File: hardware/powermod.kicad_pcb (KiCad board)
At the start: 4 copper layers, 65 x 40 mm, 78 parts, among them J1 USB_C_IN, J2 USB_C_OUT, J3 JST_PH_2, J4 STEMMA_QT, J5 SWD_HDR, Q1 AON7407, Q2 AON7407, Q3 BSS138, SW1 BUTTON, U1 BM8563, U2 PY32F003F18P6, U3 TPS63020DSJR, U4 TP4056, U5 XC6206P332MR, Y1 32.768kHz

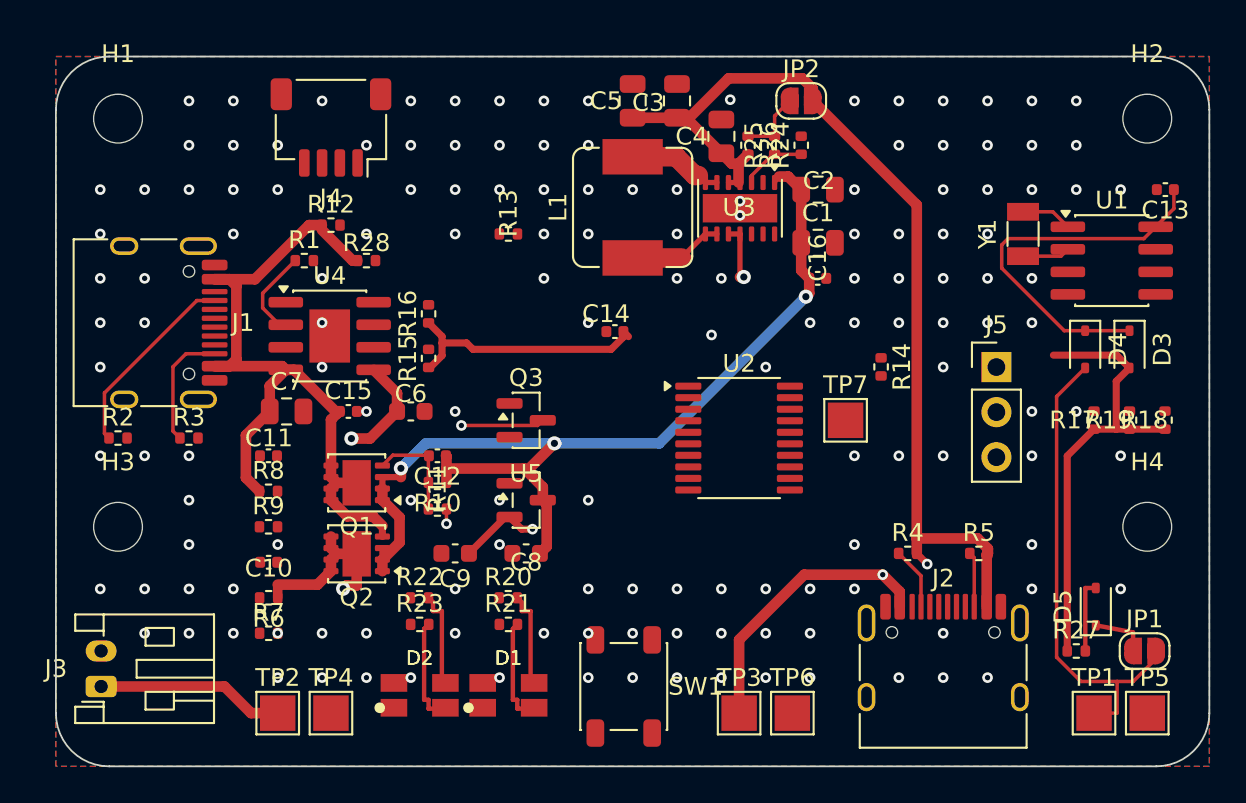
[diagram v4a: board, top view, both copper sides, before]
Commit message: hardware: user MCU/J3 placement + fix J3-flip VBAT short
User placed the TSSOP (36.5,22.5) and moved/rotated J3 to the exposed strip
(7.95,33). Flipping J3 swapped its pads, so the stale VBAT stubs to the old J3
spot shorted to the new GND pad — stripped those 6 tracks/vias. Board verified:
pad-diff 226/226, no courtyard collisions, DRC clean apart from the 4 known U3
track_width necks + 38 unrouted (MCU nets + J3 VBAT/GND). MCU-area routing TBD.

Co-Authored-By: Claude Opus 4.8 <noreply@anthropic.com>
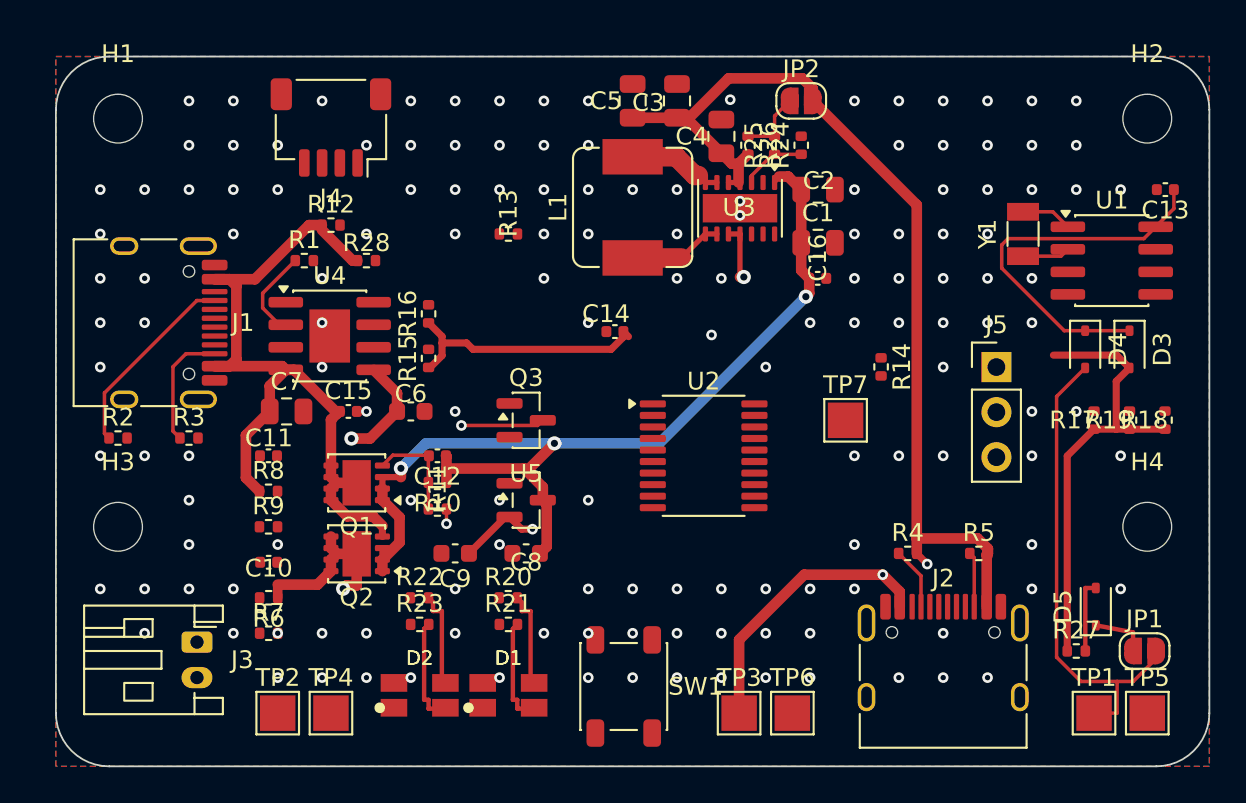
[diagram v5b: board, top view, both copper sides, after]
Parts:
- moved J3 5.95 mm to (7.95, 33.0), turned to -90 degrees
- moved U2 2.24 mm to (36.5, 22.5)
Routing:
- net VBAT: track 51.3 -> 24.8 mm
- net GND: vias 149 -> 148
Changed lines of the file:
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@@
 	(footprint "TSSOP-20_4.4x6.5mm_P0.65mm"
 		(layer "F.Cu")
-		(at 38.5 21.5)
+		(at 36.5 22.5)
 		(descr "TSSOP, 20 Pin (JEDEC MO-153 Var AC https://www.jedec.org/document_search?search_api_views_fulltext=MO-153)")
 		(tags "TSSOP SO")
@@
 	(footprint "JST_PH_S2B-PH-K_1x02_P2.00mm_Horizontal"
 		(layer "F.Cu")
-		(at 2.55 35.5 90)
+		(at 7.95 33 -90)
 		(descr "JST PH series connector, S2B-PH-K (http://www.jst-mfg.com/product/pdf/eng/ePH.pdf)")
 		(tags "connector JST PH horizontal")
@@
 		(duplicate_pad_numbers_are_jumpers no)
 		(fp_line
-			(start 4.06 -1.46)
-			(end 3.14 -1.46)
+			(start -2.06 6.36)
+			(end 4.06 6.36)
 			(stroke
 				(width 0.12)
@@
 		)
 		(fp_line
-			(start 3.14 -1.46)
-			(end 3.14 0.14)
+			(start 0.5 6.36)
+			(end 0.5 2)
 			(stroke
 				(width 0.12)
@@
 		)
 		(fp_line
-			(start -1.14 -1.46)
-			(end -2.06 -1.46)
+			(start 4.06 6.36)
+			(end 4.06 -1.46)
 			(stroke
 				(width 0.12)
@@
 		)
 		(fp_line
-			(start -2.06 -1.46)
-			(end -2.06 6.36)
+			(start -0.8 4.1)
+			(end -0.8 6.36)
 			(stroke
 				(width 0.12)
@@
 		)
 		(fp_line
-			(start 4.06 0.14)
-			(end 3.14 0.14)
+			(start -0.3 4.1)
+			(end -0.3 6.36)
 			(stroke
 				(width 0.12)
@@
 		)
 		(fp_line
-			(start 3.14 0.14)
-			(end 2.86 0.14)
+			(start 0.5 2)
+			(end 1.5 2)
 			(stroke
 				(width 0.12)
@@
 		)
 		(fp_line
-			(start -0.86 0.14)
-			(end -0.86 -1.075)
+			(start 1.5 2)
+			(end 1.5 6.36)
 			(stroke
 				(width 0.12)
@@
 		)
 		(fp_line
-			(start -0.86 0.14)
+			(start -2.06 0.14)
 			(end -1.14 0.14)
 			(stroke
@@
 		)
 		(fp_line
-			(start -2.06 0.14)
+			(start -0.86 0.14)
 			(end -1.14 0.14)
 			(stroke
@@
 		)
 		(fp_line
-			(start 1.5 2)
-			(end 1.5 6.36)
+			(start -0.86 0.14)
+			(end -0.86 -1.075)
 			(stroke
 				(width 0.12)
@@
 		)
 		(fp_line
-			(start 0.5 2)
-			(end 1.5 2)
+			(start 3.14 0.14)
+			(end 2.86 0.14)
 			(stroke
 				(width 0.12)
@@
 		)
 		(fp_line
-			(start -0.3 4.1)
-			(end -0.3 6.36)
+			(start 4.06 0.14)
+			(end 3.14 0.14)
 			(stroke
 				(width 0.12)
@@
 		)
 		(fp_line
-			(start -0.8 4.1)
-			(end -0.8 6.36)
+			(start -2.06 -1.46)
+			(end -2.06 6.36)
 			(stroke
 				(width 0.12)
@@
 		)
 		(fp_line
-			(start 4.06 6.36)
-			(end 4.06 -1.46)
+			(start -1.14 -1.46)
+			(end -2.06 -1.46)
 			(stroke
 				(width 0.12)
@@
 		)
 		(fp_line
-			(start 0.5 6.36)
-			(end 0.5 2)
+			(start 3.14 -1.46)
+			(end 3.14 0.14)
 			(stroke
 				(width 0.12)
@@
 		)
 		(fp_line
-			(start -2.06 6.36)
-			(end 4.06 6.36)
+			(start 4.06 -1.46)
+			(end 3.14 -1.46)
 			(stroke
 				(width 0.12)
@@
 		)
 		(fp_rect
-			(start 2.3 2.5)
-			(end 3.3 4.1)
+			(start -1.3 2.5)
+			(end -0.3 4.1)
 			(stroke
 				(width 0.12)
@@
 		)
 		(fp_rect
-			(start -1.3 2.5)
-			(end -0.3 4.1)
+			(start 2.3 2.5)
+			(end 3.3 4.1)
 			(stroke
 				(width 0.12)
@@
 		)
 		(fp_line
-			(start 3.95 -1.35)
-			(end 3.25 -1.35)
+			(start -1.95 6.25)
+			(end 3.95 6.25)
 			(stroke
 				(width 0.1)
@@
 		)
 		(fp_line
-			(start 3.25 -1.35)
-			(end 3.25 0.25)
+			(start 3.95 6.25)
+			(end 3.95 -1.35)
 			(stroke
 				(width 0.1)
@@
 		)
 		(fp_line
-			(start -1.25 -1.35)
-			(end -1.95 -1.35)
+			(start -0.5 1.375)
+			(end 0.5 1.375)
 			(stroke
 				(width 0.1)
@@
 		)
 		(fp_line
-			(start -1.95 -1.35)
-			(end -1.95 6.25)
+			(start 0.5 1.375)
+			(end 0 0.875)
 			(stroke
 				(width 0.1)
@@
 		)
 		(fp_line
-			(start 3.25 0.25)
-			(end -1.25 0.25)
+			(start 0 0.875)
+			(end -0.5 1.375)
 			(stroke
 				(width 0.1)
@@
 		)
 		(fp_line
-			(start 0 0.875)
-			(end -0.5 1.375)
+			(start 3.25 0.25)
+			(end -1.25 0.25)
 			(stroke
 				(width 0.1)
@@
 		)
 		(fp_line
-			(start 0.5 1.375)
-			(end 0 0.875)
+			(start -1.95 -1.35)
+			(end -1.95 6.25)
 			(stroke
 				(width 0.1)
@@
 		)
 		(fp_line
-			(start -0.5 1.375)
-			(end 0.5 1.375)
+			(start -1.25 -1.35)
+			(end -1.95 -1.35)
 			(stroke
 				(width 0.1)
@@
 		)
 		(fp_line
-			(start 3.95 6.25)
-			(end 3.95 -1.35)
+			(start 3.25 -1.35)
+			(end 3.25 0.25)
 			(stroke
 				(width 0.1)
@@
 		)
 		(fp_line
-			(start -1.95 6.25)
-			(end 3.95 6.25)
+			(start 3.95 -1.35)
+			(end 3.25 -1.35)
 			(stroke
 				(width 0.1)
@@
 		)
 		(pad "1" thru_hole roundrect
-			(at 0 0 90)
+			(at 0 0 270)
 			(size 1.2 1.75)
 			(drill 0.75)
@@
 		)
 		(pad "2" thru_hole oval
-			(at 2 0 90)
+			(at 2 0 270)
 			(size 1.2 1.75)
 			(drill 0.75)
@@
 	)
 	(via
-		(at 7.5 32.5)
-		(size 0.6)
-		(drill 0.3)
-		(layers "F.Cu" "B.Cu")
-		(net "GND")
-	)
-	(via
 		(at 45 30)
 		(size 0.6)
@@
 	)
 	(segment
-		(start 2.55 35.5)
-		(end 9.4983 35.5)
-		(width 0.6)
-		(layer "F.Cu")
-		(net "VBAT")
-	)
-	(segment
-		(start 9.4983 35.5)
-		(end 10.9983 37)
-		(width 0.6)
-		(layer "F.Cu")
-		(net "VBAT")
-	)
-	(segment
 		(start 12.5 29.7607)
 		(end 12.5 30.5)
@@
 	)
 	(segment
-		(start 12.5 37)
-		(end 10.9983 37)
-		(width 0.6)
-		(layer "F.Cu")
-		(net "VBAT")
-	)
-	(segment
 		(start 17.6973 21.5277)
 		(end 16.6533 21.5277)
@@
 	)
 	(segment
-		(start 2.55 35.5)
-		(end 10.677 35.5)
-		(width 0.6)
-		(layer "In2.Cu")
-		(net "VBAT")
-	)
-	(segment
 		(start 16.6533 21.5277)
 		(end 16.6533 29.5237)
 		(width 0.6)
 		(layer "In2.Cu")
-		(net "VBAT")
-	)
-	(segment
-		(start 10.677 35.5)
-		(end 16.1871 29.9899)
-		(width 0.6)
-		(layer "In2.Cu")

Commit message: hardware: full Freerouting reroute for the PY32F003 board
Option B: strip-and-reroute the whole board (grid A* + incremental Freerouting
both can't thread the MCU corner; Freerouting crashes on pre-routed input, so
full reroute is the only viable autoroute). Freerouting v2.2.4 -mp 50:
121 -> 6 unrouted. finish_board: SES import + 136 GND stitch vias + 2 island
ties -> 382 tracks, 181 vias.

DRC clean apart from the 4 known U3 track_width necks. Pad-diff 226/226.
6 connections remain: the USB-C large power pads (VBUS->J1 A4/A9, VOUT->J2
A4/A9 + TP3) — the known "scripted/auto tracks don't bind to big connector
pads" case; hand-route these (and re-apply the VBUS A9/A4 current-share split).
NOTE: all routing is Freerouting's, not the prior hand-tuned power/USB.

Co-Authored-By: Claude Opus 4.8 <noreply@anthropic.com>
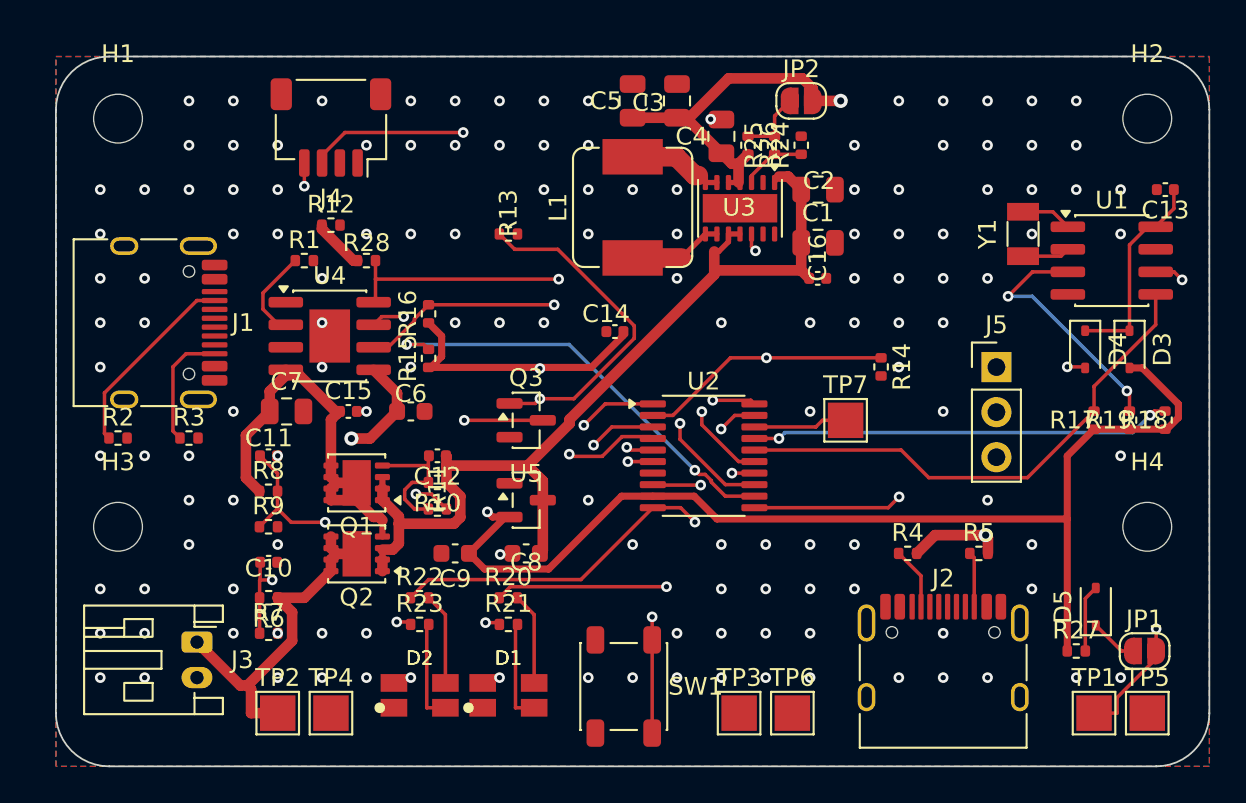
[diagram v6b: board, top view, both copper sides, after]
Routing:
- net LED_BAT_B: track 0.00 -> 51.3 mm, vias 0 -> 2
- net RTC_INT: track 0.00 -> 38.5 mm, vias 0 -> 3
- net LED_BAT_A: track 0.00 -> 37.0 mm, vias 0 -> 1
- net SDA: track 0.00 -> 35.6 mm, vias 0 -> 2
- net SCL: track 0.00 -> 35.4 mm, vias 0 -> 2
- net RTC_SCL: track 0.00 -> 33.8 mm, vias 0 -> 3
- net VBAT_DIV: track 0.00 -> 29.7 mm, vias 0 -> 2
- net RTC_SDA: track 0.00 -> 29.4 mm
- net VBUS_DIV: track 0.00 -> 28.5 mm, vias 0 -> 2
- net CHG_CHRG: track 0.00 -> 28.1 mm, vias 0 -> 3
- net Q1_GATE_DRV: track 0.00 -> 26.5 mm, vias 0 -> 2
- net CHG_CE: track 0.00 -> 25.3 mm, vias 0 -> 2
- net CHG_STDBY: track 0.00 -> 23.3 mm, vias 0 -> 2
- net LED_PWR_B: track 0.00 -> 22.7 mm, vias 0 -> 2
- net BUTTON: track 0.00 -> 22.6 mm, vias 0 -> 2
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
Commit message: hardware: complete board routing + regenerate CPL
Hand-routed the 6 USB-C large-pad escapes (VBUS->J1 A4/A9, VOUT->J2 A4/A9,
VOUT->TP3) at 0.6mm. Board now: 0 unrouted, 0 clearance, pad-diff 226/226.
Only the 4 known U3 track_width necks remain on copper. Remaining DRC items
are silkscreen warnings (ref-des over copper/overlap) — cosmetic, fab-clipped.
CPL regenerated from final placement (65 placements).

Co-Authored-By: Claude Opus 4.8 <noreply@anthropic.com>
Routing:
- net VOUT: track 55.0 -> 77.2 mm
- net VBUS: track 25.8 -> 44.1 mm
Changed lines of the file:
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@@
+	)
+	(segment
+		(start 11.081371 12.55)
+		(end 14.131371 9.5)
+		(width 0.6)
+		(layer "F.Cu")
+		(net "VBUS")
 	)
 	(segment
@@
 	)
 	(segment
+		(start 8.945 17.45)
+		(end 12.75 17.45)
+		(width 0.6)
+		(layer "F.Cu")
+		(net "VBUS")
+	)
+	(segment
 		(start 16.99 11.5)
 		(end 16.7667 11.5)
@@
 	)
 	(segment
+		(start 12.75 17.45)
+		(end 12.955 17.655)
+		(width 0.6)
+		(layer "F.Cu")
+		(net "VBUS")
+	)
+	(segment
+		(start 9.785252 17.45)
+		(end 10.17 17.065252)
+		(width 0.6)
+		(layer "F.Cu")
+		(net "VBUS")
+	)
+	(segment
 		(start 15.825 24.025)
 		(end 15.5 23.7)
@@
 	)
 	(segment
+		(start 14.131371 9.5)
+		(end 14.99 9.5)
+		(width 0.6)
+		(layer "F.Cu")
+		(net "VBUS")
+	)
+	(segment
 		(start 10.7086 23.7386)
 		(end 10.7086 21.3414)
@@
 		(start 15.5 25)
 		(end 15.5 24.35)
+		(width 0.6)
+		(layer "F.Cu")
+		(net "VBUS")
+	)
+	(segment
+		(start 8.945 12.55)
+		(end 11.081371 12.55)
 		(width 0.6)
 		(layer "F.Cu")
@@
 	)
 	(segment
+		(start 8.945 17.45)
+		(end 9.785252 17.45)
+		(width 0.6)
+		(layer "F.Cu")
+		(net "VBUS")
+	)
+	(segment
+		(start 10.17 12.934748)
+		(end 9.785252 12.55)
+		(width 0.6)
+		(layer "F.Cu")
+		(net "VBUS")
+	)
+	(segment
+		(start 10.17 17.065252)
+		(end 10.17 12.934748)
+		(width 0.6)
+		(layer "F.Cu")
+		(net "VBUS")
+	)
+	(segment
+		(start 9.785252 12.55)
+		(end 8.945 12.55)
+		(width 0.6)
+		(layer "F.Cu")
+		(net "VBUS")
+	)
+	(segment
 		(start 10.7086 21.3414)
 		(end 12.05 20)
@@
 	)
 	(segment
+		(start 38.5 35.368629)
+		(end 45.868629 28)
+		(width 0.6)
+		(layer "F.Cu")
+		(net "VOUT")
+	)
+	(segment
 		(start 38.55 7.1)
 		(end 38.4687 7.1)
@@
 	)
 	(segment
+		(start 46.72 28)
+		(end 46.72 27.548232)
+		(width 0.6)
+		(layer "F.Cu")
+		(net "VOUT")
+	)
+	(segment
 		(start 42.65 2.5)
 		(end 44.2234 2.5)
@@
 	)
 	(segment
+		(start 48.51 27.680001)
+		(end 48.51 28)
+		(width 0.6)
+		(layer "F.Cu")
+		(net "VOUT")
+	)
+	(segment
 		(start 42.0717 1.2326)
 		(end 42.65 1.8109)
@@
 	)
 	(segment
+		(start 52.45 28.07)
+		(end 52.52 28)
+		(width 0.6)
+		(layer "F.Cu")
+		(net "VOUT")
+	)
+	(segment
 		(start 38.4687 6.0413)
 		(end 38.0913 6.0413)
@@
 	)
 	(segment
+		(start 47.55 31.005)
+		(end 47.55 29.281768)
+		(width 0.6)
+		(layer "F.Cu")
+		(net "VOUT")
+	)
+	(segment
 		(start 52.52 27.0959)
 		(end 52.52 28)
@@
 	)
 	(segment
+		(start 52.45 31.005)
+		(end 52.45 28.07)
+		(width 0.6)
+		(layer "F.Cu")
+		(net "VOUT")
+	)
+	(segment
 		(start 35.0349 3.4849)
 		(end 35 3.45)
@@
 	)
 	(segment
+		(start 46.72 27.548232)
+		(end 47.088232 27.18)
+		(width 0.6)
+		(layer "F.Cu")
+		(net "VOUT")
+	)
+	(segment
+		(start 47.55 29.281768)
+		(end 46.72 28.451768)
+		(width 0.6)
+		(layer "F.Cu")
+		(net "VOUT")
+	)
+	(segment
 		(start 48.51 28)
 		(end 49.5401 26.9699)
@@
 	)
 	(segment
+		(start 45.868629 28)
+		(end 46.72 28)
+		(width 0.6)
+		(layer "F.Cu")
+		(net "VOUT")
+	)
+	(segment
 		(start 42.65 1.8109)
 		(end 42.65 2.5)
+		(width 0.6)
+		(layer "F.Cu")
+		(net "VOUT")
+	)
+	(segment
+		(start 46.72 28.451768)
+		(end 46.72 28)
 		(width 0.6)
 		(layer "F.Cu")
@@
 	)
 	(segment
+		(start 47.088232 27.18)
+		(end 48.009999 27.18)
+		(width 0.6)
+		(layer "F.Cu")
+		(net "VOUT")
+	)
+	(segment
 		(start 35.6566 3.4849)
 		(end 35.0349 3.4849)
@@
 		(width 0.6)
 		(layer "F.Cu")
+		(net "VOUT")
+	)
+	(segment
+		(start 48.009999 27.18)
+		(end 48.51 27.680001)
+		(width 0.6)
+		(layer "F.Cu")
+		(net "VOUT")
+	)
+	(segment
+		(start 38.5 37)
+		(end 38.5 35.368629)
+		(width 0.6)
+		(layer "F.Cu")

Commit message: hardware: J5 3-pin+TP7 -> 4-pin SWD header (NRST folded in) [WIP]
Fold the NRST probe pad (TP7) into J5 as a 4th header pin: J5 1x03 -> 1x04
(GND/SWCLK/SWDIO/NRST), TP7 removed, NRST net now U2.18 + J5.4. Cleaner
programming connector (proper connect-under-reset pin, no loose test pad).

WIP: J5's default in-place spot puts pin 4 over routed copper (a GND stitch via
+ VOUT/3V3 traces). User repositions J5 to a clear area next; then reroute its
4 connections + refill + DRC + regen CPL/gerbers. pad-diff 226/226.

Co-Authored-By: Claude Opus 4.8 <noreply@anthropic.com>
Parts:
- removed TP7: NRST_PAD, TestPoint_Pad_2.0x2.0mm
- J5: footprint PinHeader_1x03_P2.54mm_Vertical -> PinHeader_1x04_P2.54mm_Vertical
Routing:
- net NRST: track 5.29 -> 0.00 mm
